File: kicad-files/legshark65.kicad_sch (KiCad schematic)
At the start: 160 parts, among them J1 ARM JTAG, SW1 K2-1187SQ-A4SW-06, SW2 PCM12SMTR, T2 53261-0471, U1 STM32F411CEU6, U3 AT24C256C-SSHL-T, Y1 TAXM8M4RFDCET2T

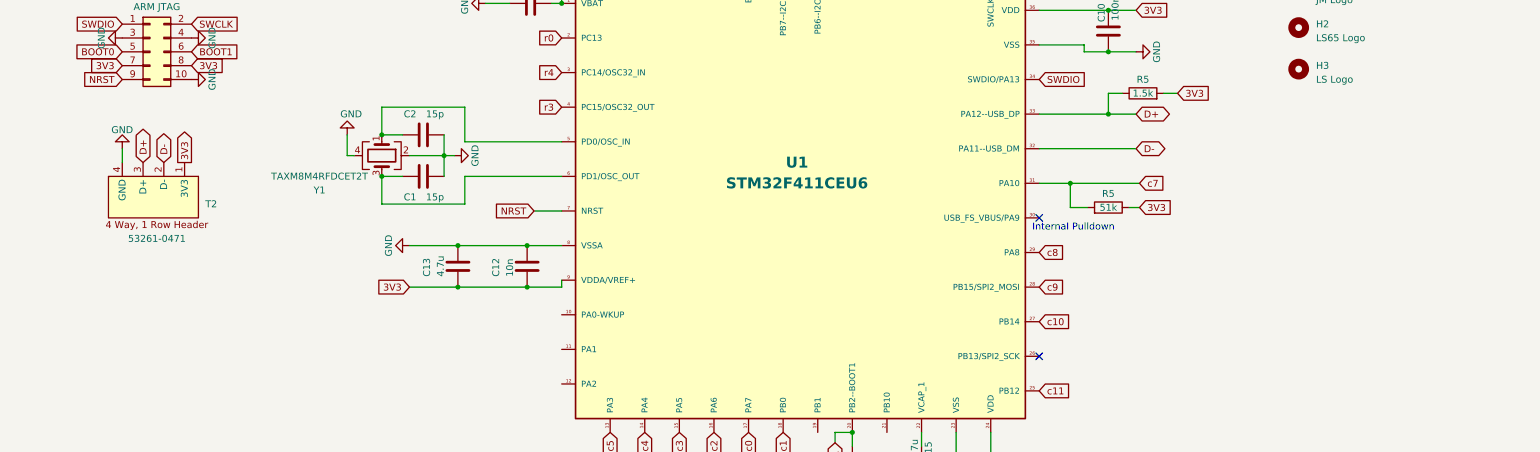
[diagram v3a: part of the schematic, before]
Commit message: Finished add BOM to motherboard & fixing some small parts
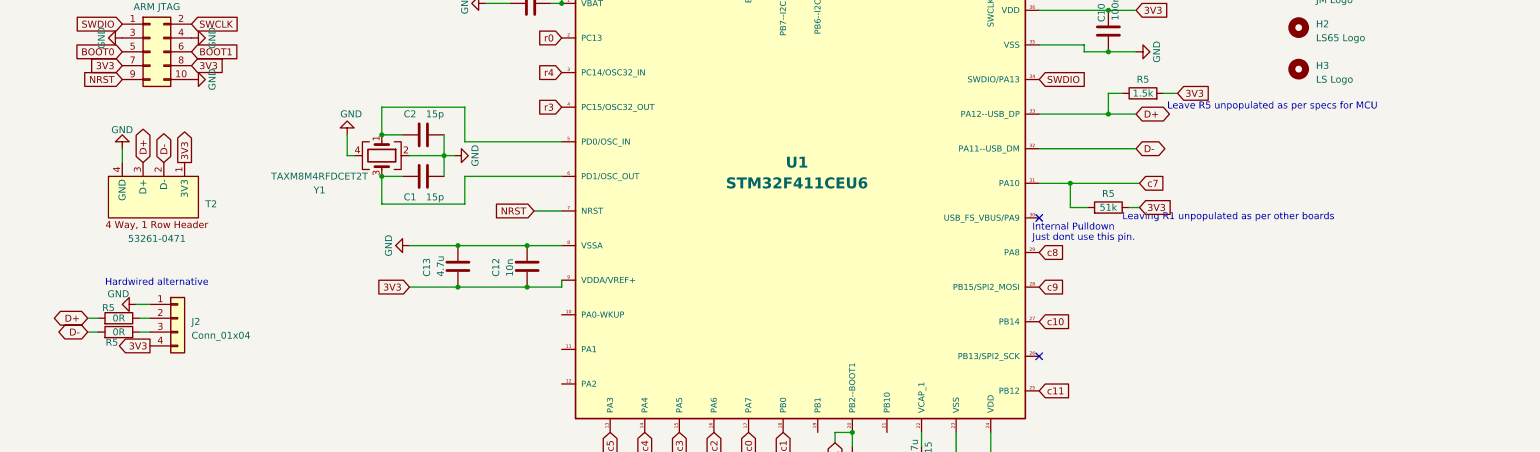
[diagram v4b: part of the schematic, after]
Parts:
- added J2: Conn_01x04, acheron_Connectors:PinHeader_1x4_P2.54mm_Vertical, symbol Connector_Generic:Conn_01x04
- added R5 (x2): 0R, Resistor_SMD:R_0603_1608Metric, symbol Device:R
- R11: LCSC Part (none) -> C22775; Manufacturer (none) -> Uniroyal Elec; Manufacturer Part Number (none) -> 0603WAF1000T5E; Package (none) -> 0603; Specification (none) -> ±1% 100Ω 0603 Chip Resistor; Vendor Part Number (none) -> LCSC C22775
- R15, R6: LCSC Part (none) -> C25804; Manufacturer (none) -> Uniroyal Elec; Manufacturer Part Number (none) -> 0603WAF1002T5E; Package (none) -> 0603; Specification (none) -> ±1% 10kΩ 0603 Chip Resistor; Vendor Part Number (none) -> LCSC C25804
- R7, R8: LCSC Part (none) -> C23162; Manufacturer (none) -> Uniroyal Elec; Manufacturer Part Number (none) -> 0603WAF4701T5E; Package (none) -> 0603; Specification (none) -> ±1% 4.7kΩ 0603 Chip Resistor; Vendor Part Number (none) -> LCSC C23162
- SW1: LCSC Part (none) -> C92584
- SW2: Manufacturer Part Number (none) -> PCM12SMTR; Vendor Part Number C221841 -> LCSC C221841
- U1: LCSC Part (none) -> C60420; Specification (none) -> 32-bit ARM Cortex-M0+ 128kBytes flash microcontroller
- U3: LCSC Part (none) -> C6482
- Y1: LCSC Part (none) -> C403948
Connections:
- net 3V3: now also J2.4 (Pin_4)
- net D+: now also R5.2
- net D-: now also R5.2
- net GND: now also J2.1 (Pin_1)
- new net: J2.2 (Pin_2), R5.1
- new net: J2.3 (Pin_3), R5.1
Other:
- note added: "Hardwired alternative"
- note added: "Just dont use this pin."
- note added: "Leave R5 unpopulated as per specs for MCU"
- note added: "Leaving R1 unpopulated as per other boards"

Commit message: Updated PCB and schematic to v2.2 layout
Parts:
- K_57: footprint MX_Only:MXOnly-1.75U-NoLED -> MX_Only:MXOnly-1.25U-NoLED
- K_60: footprint MX_Only:MXOnly-2.25U-ReversedStabilizers-NoLED -> MX_Only:MXOnly-2.75U-ReversedStabilizers-NoLED
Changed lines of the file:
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@@
       (effects (font (size 1.524 1.524)) hide)
     )
-    (property "Footprint" "MX_Only:MXOnly-1.75U-NoLED" (at 52.705 137.795 0)
+    (property "Footprint" "MX_Only:MXOnly-1.25U-NoLED" (at 52.705 137.795 0)
       (effects (font (size 1.524 1.524)) hide)
     )
@@
       (effects (font (size 1.524 1.524)) hide)
     )
-    (property "Footprint" "MX_Only:MXOnly-2.25U-ReversedStabilizers-NoLED" (at 179.705 137.795 0)
-      (effects (font (size 1.524 1.524)) hide)
-    )
+    (property "Footprint" "MX_Only:MXOnly-2.75U-ReversedStabilizers-NoLED" (at 179.705 137.795 0)
+      (effects (font (size 1.524 1.524)) hide)
+    )

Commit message: Made some very slight changes as per processing
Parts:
- C13, C15: LCSC Part C2857987 -> C108342; Vendor Part Number LCSC C2857987 -> LCSC C108342
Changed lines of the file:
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@@
       (effects (font (size 1.27 1.27)) hide)
     )
-    (property "LCSC Part" "C2857987" (at 107.95 275.59 0)
+    (property "LCSC Part" "C108342" (at 107.95 275.59 0)
       (effects (font (size 1.27 1.27)) hide)
     )
@@
       (effects (font (size 1.27 1.27)) hide)
     )
-    (property "Vendor Part Number" "LCSC C2857987" (at 107.95 275.59 0)
+    (property "Vendor Part Number" "LCSC C108342" (at 107.95 275.59 0)
       (effects (font (size 1.27 1.27)) hide)
     )
@@
       (effects (font (size 1.27 1.27)) hide)
     )
-    (property "LCSC Part" "C2857987" (at 193.04 312.42 0)
+    (property "LCSC Part" "C108342" (at 193.04 312.42 0)
       (effects (font (size 1.27 1.27)) hide)
     )
@@
       (effects (font (size 1.27 1.27)) hide)
     )
-    (property "Vendor Part Number" "LCSC C2857987" (at 193.04 312.42 0)
-      (effects (font (size 1.27 1.27)) hide)
-    )
+    (property "Vendor Part Number" "LCSC C108342" (at 193.04 312.42 0)
+      (effects (font (size 1.27 1.27)) hide)
+    )
